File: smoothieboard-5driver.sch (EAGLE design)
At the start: 283 parts, among them IC1 LPC1769, IC10 LM1117-3.3V, IC11 78L12F, IC12 A4982, IC13 R-78E-5.0, IC2 A4982, IC3 A4982, IC4 MCP44X1, IC5 A4982, IC6 A4982, IC9 MCP44X1, J10 POWER_JACKSMD, Q1 BSL207SP, Q10 SUD50P04-08-GE3, Q2 12MHz, Q3 25MHz, Q4 ZXMN4A06, Q5 AOT240L, Q6 AOT240L, Q7 AOT240L, Q8 ZXMN4A06, Q9 ZXMN4A06, U1 USD-SOCKETNEW, X14 USBPTH

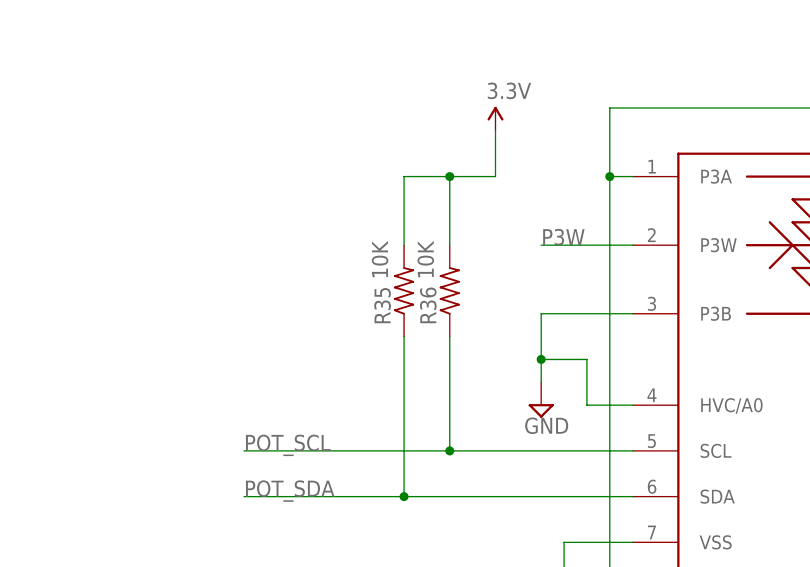
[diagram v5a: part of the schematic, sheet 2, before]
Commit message: reduce I2C pull-up resistors to 2.2k
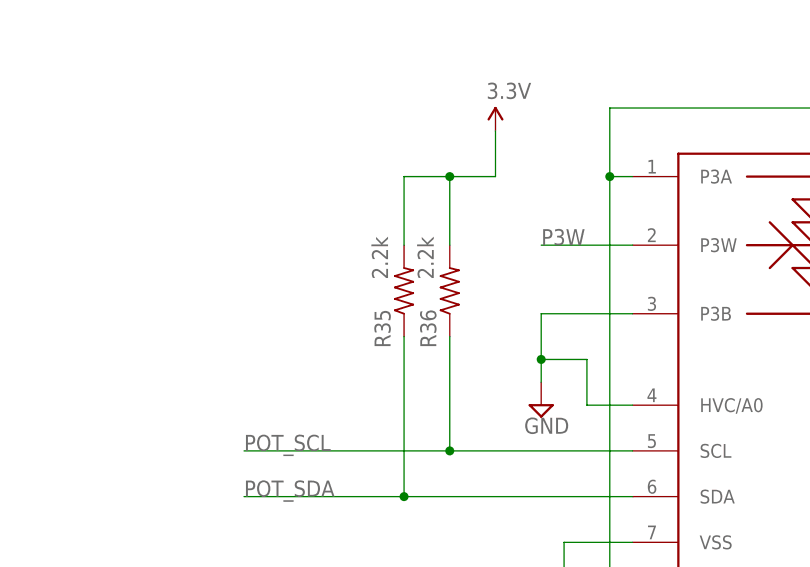
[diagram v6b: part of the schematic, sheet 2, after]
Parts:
- R35, R36, R5, R6: value 10K -> 2.2k
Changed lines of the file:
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@@
 <grid distance="0.1" unitdist="inch" unit="inch" style="lines" multiple="1" display="no" altdistance="0.01" altunitdist="inch" altunit="inch"/>
 <layers>
-<layer number="1" name="Top" color="4" fill="1" visible="yes" active="no"/>
-<layer number="2" name="Route2" color="2" fill="1" visible="yes" active="no"/>
-<layer number="3" name="Route3" color="4" fill="3" visible="yes" active="no"/>
-<layer number="4" name="Route4" color="1" fill="4" visible="yes" active="no"/>
-<layer number="5" name="Route5" color="4" fill="4" visible="yes" active="no"/>
-<layer number="6" name="Route6" color="1" fill="8" visible="yes" active="no"/>
-<layer number="7" name="Route7" color="4" fill="8" visible="yes" active="no"/>
-<layer number="8" name="Route8" color="1" fill="2" visible="yes" active="no"/>
-<layer number="9" name="Route9" color="4" fill="2" visible="yes" active="no"/>
-<layer number="10" name="Route10" color="1" fill="7" visible="yes" active="no"/>
-<layer number="11" name="Route11" color="4" fill="7" visible="yes" active="no"/>
-<layer number="12" name="Route12" color="1" fill="5" visible="yes" active="no"/>
-<layer number="13" name="Route13" color="4" fill="5" visible="yes" active="no"/>
-<layer number="14" name="Route14" color="1" fill="6" visible="yes" active="no"/>
-<layer number="15" name="Route15" color="5" fill="1" visible="yes" active="no"/>
-<layer number="16" name="Bottom" color="1" fill="1" visible="yes" active="no"/>
-<layer number="17" name="Pads" color="2" fill="1" visible="yes" active="no"/>
-<layer number="18" name="Vias" color="6" fill="1" visible="yes" active="no"/>
-<layer number="19" name="Unrouted" color="6" fill="1" visible="yes" active="no"/>
-<layer number="20" name="Dimension" color="15" fill="1" visible="yes" active="no"/>
-<layer number="21" name="tPlace" color="7" fill="1" visible="yes" active="no"/>
-<layer number="22" name="bPlace" color="7" fill="1" visible="yes" active="no"/>
-<layer number="23" name="tOrigins" color="15" fill="1" visible="yes" active="no"/>
-<layer number="24" name="bOrigins" color="15" fill="1" visible="yes" active="no"/>
-<layer number="25" name="tNames" color="7" fill="1" visible="yes" active="no"/>
-<layer number="26" name="bNames" color="7" fill="1" visible="yes" active="no"/>
-<layer number="27" name="tValues" color="7" fill="1" visible="yes" active="no"/>
-<layer number="28" name="bValues" color="7" fill="1" visible="yes" active="no"/>
+<layer number="1" name="Top" color="4" fill="1" visible="no" active="no"/>
+<layer number="2" name="Route2" color="2" fill="1" visible="no" active="no"/>
+<layer number="3" name="Route3" color="4" fill="3" visible="no" active="no"/>
+<layer number="4" name="Route4" color="1" fill="4" visible="no" active="no"/>
+<layer number="5" name="Route5" color="4" fill="4" visible="no" active="no"/>
+<layer number="6" name="Route6" color="1" fill="8" visible="no" active="no"/>
+<layer number="7" name="Route7" color="4" fill="8" visible="no" active="no"/>
+<layer number="8" name="Route8" color="1" fill="2" visible="no" active="no"/>
+<layer number="9" name="Route9" color="4" fill="2" visible="no" active="no"/>
+<layer number="10" name="Route10" color="1" fill="7" visible="no" active="no"/>
+<layer number="11" name="Route11" color="4" fill="7" visible="no" active="no"/>
+<layer number="12" name="Route12" color="1" fill="5" visible="no" active="no"/>
+<layer number="13" name="Route13" color="4" fill="5" visible="no" active="no"/>
+<layer number="14" name="Route14" color="1" fill="6" visible="no" active="no"/>
+<layer number="15" name="Route15" color="5" fill="1" visible="no" active="no"/>
+<layer number="16" name="Bottom" color="1" fill="1" visible="no" active="no"/>
+<layer number="17" name="Pads" color="2" fill="1" visible="no" active="no"/>
+<layer number="18" name="Vias" color="6" fill="1" visible="no" active="no"/>
+<layer number="19" name="Unrouted" color="6" fill="1" visible="no" active="no"/>
+<layer number="20" name="Dimension" color="15" fill="1" visible="no" active="no"/>
+<layer number="21" name="tPlace" color="7" fill="1" visible="no" active="no"/>
+<layer number="22" name="bPlace" color="7" fill="1" visible="no" active="no"/>
+<layer number="23" name="tOrigins" color="15" fill="1" visible="no" active="no"/>
+<layer number="24" name="bOrigins" color="15" fill="1" visible="no" active="no"/>
+<layer number="25" name="tNames" color="7" fill="1" visible="no" active="no"/>
+<layer number="26" name="bNames" color="7" fill="1" visible="no" active="no"/>
+<layer number="27" name="tValues" color="7" fill="1" visible="no" active="no"/>
+<layer number="28" name="bValues" color="7" fill="1" visible="no" active="no"/>
 <layer number="29" name="tStop" color="7" fill="3" visible="no" active="no"/>
 <layer number="30" name="bStop" color="7" fill="6" visible="no" active="no"/>
@@
 <layer number="35" name="tGlue" color="7" fill="4" visible="no" active="no"/>
 <layer number="36" name="bGlue" color="7" fill="5" visible="no" active="no"/>
-<layer number="37" name="tTest" color="7" fill="1" visible="yes" active="no"/>
-<layer number="38" name="bTest" color="7" fill="1" visible="yes" active="no"/>
+<layer number="37" name="tTest" color="7" fill="1" visible="no" active="no"/>
+<layer number="38" name="bTest" color="7" fill="1" visible="no" active="no"/>
 <layer number="39" name="tKeepout" color="4" fill="11" visible="no" active="no"/>
 <layer number="40" name="bKeepout" color="1" fill="11" visible="no" active="no"/>
@@
 <layer number="44" name="Drills" color="7" fill="1" visible="no" active="no"/>
 <layer number="45" name="Holes" color="7" fill="1" visible="no" active="no"/>
-<layer number="46" name="Milling" color="3" fill="1" visible="yes" active="no"/>
-<layer number="47" name="Measures" color="7" fill="1" visible="yes" active="no"/>
-<layer number="48" name="Document" color="7" fill="1" visible="yes" active="no"/>
-<layer number="49" name="Reference" color="7" fill="1" visible="yes" active="no"/>
-<layer number="50" name="dxf" color="7" fill="1" visible="yes" active="no"/>
-<layer number="51" name="tDocu" color="7" fill="1" visible="yes" active="no"/>
-<layer number="52" name="bDocu" color="7" fill="1" visible="yes" active="no"/>
-<layer number="53" name="tGND_GNDA" color="7" fill="9" visible="yes" active="no"/>
-<layer number="54" name="bGND_GNDA" color="1" fill="9" visible="yes" active="no"/>
-<layer number="56" name="wert" color="7" fill="1" visible="yes" active="no"/>
+<layer number="46" name="Milling" color="3" fill="1" visible="no" active="no"/>
+<layer number="47" name="Measures" color="7" fill="1" visible="no" active="no"/>
+<layer number="48" name="Document" color="7" fill="1" visible="no" active="no"/>
+<layer number="49" name="Reference" color="7" fill="1" visible="no" active="no"/>
+<layer number="50" name="dxf" color="7" fill="1" visible="no" active="no"/>
+<layer number="51" name="tDocu" color="7" fill="1" visible="no" active="no"/>
+<layer number="52" name="bDocu" color="7" fill="1" visible="no" active="no"/>
+<layer number="53" name="tGND_GNDA" color="7" fill="9" visible="no" active="no"/>
+<layer number="54" name="bGND_GNDA" color="1" fill="9" visible="no" active="no"/>
+<layer number="56" name="wert" color="7" fill="1" visible="no" active="no"/>
 <layer number="91" name="Nets" color="2" fill="1" visible="yes" active="yes"/>
 <layer number="92" name="Busses" color="1" fill="1" visible="yes" active="yes"/>
@@
 <part name="SUPPLY61" library="supply2" deviceset="GND" device=""/>
 <part name="P+30" library="SparkFun" deviceset="3.3V" device=""/>
-<part name="R5" library="resistor" deviceset="R-US_" device="R0603" value="10K"/>
-<part name="R6" library="resistor" deviceset="R-US_" device="R0603" value="10K"/>
+<part name="R5" library="resistor" deviceset="R-US_" device="R0603" value="2.2k"/>
+<part name="R6" library="resistor" deviceset="R-US_" device="R0603" value="2.2k"/>
 <part name="SUPPLY64" library="supply2" deviceset="GND" device=""/>
 <part name="S1" library="SparkFun" deviceset="TAC_SWITCH" device="SMD"/>
@@
 <part name="RN1" library="resistor-dil" deviceset="4R-N" device="0603-ARV" value="4.7K"/>
 <part name="IC4" library="Geos" deviceset="MCP44X1" device=""/>
-<part name="R35" library="resistor" deviceset="R-US_" device="R0603" value="10K"/>
-<part name="R36" library="resistor" deviceset="R-US_" device="R0603" value="10K"/>
+<part name="R35" library="resistor" deviceset="R-US_" device="R0603" value="2.2k"/>
+<part name="R36" library="resistor" deviceset="R-US_" device="R0603" value="2.2k"/>
 <part name="J1" library="con-amp" deviceset="MTA04-100" device=""/>
 <part name="J2" library="con-amp" deviceset="MTA04-100" device=""/>
@@
 <instance part="IC4" gate="G$1" x="289.56" y="71.12"/>
 <instance part="R35" gate="G$1" x="259.08" y="127" smashed="yes" rot="R90">
-<attribute name="NAME" x="257.5814" y="123.19" size="1.778" layer="95" rot="R90"/>
+<attribute name="NAME" x="257.5814" y="120.65" size="1.778" layer="95" rot="R90"/>
 <attribute name="VALUE" x="257.302" y="128.27" size="1.778" layer="96" rot="R90"/>
 </instance>
 <instance part="R36" gate="G$1" x="264.16" y="127" smashed="yes" rot="R90">
-<attribute name="NAME" x="262.6614" y="123.19" size="1.778" layer="95" rot="R90"/>
+<attribute name="NAME" x="262.6614" y="120.65" size="1.778" layer="95" rot="R90"/>
 <attribute name="VALUE" x="262.382" y="128.27" size="1.778" layer="96" rot="R90"/>
 </instance>

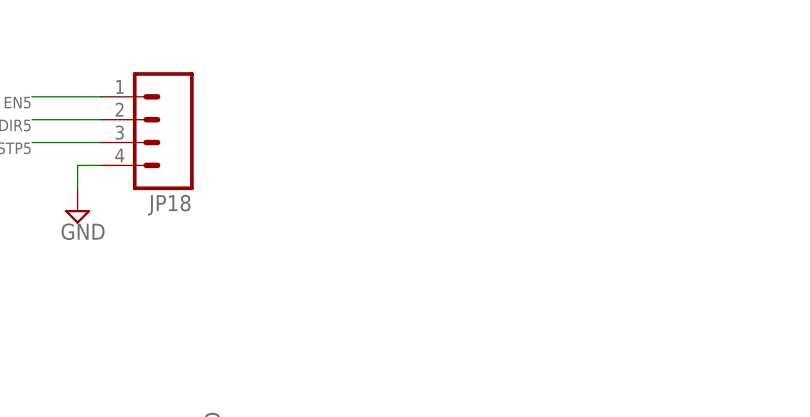
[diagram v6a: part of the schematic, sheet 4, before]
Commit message: Break out digipot I2C bus to a header
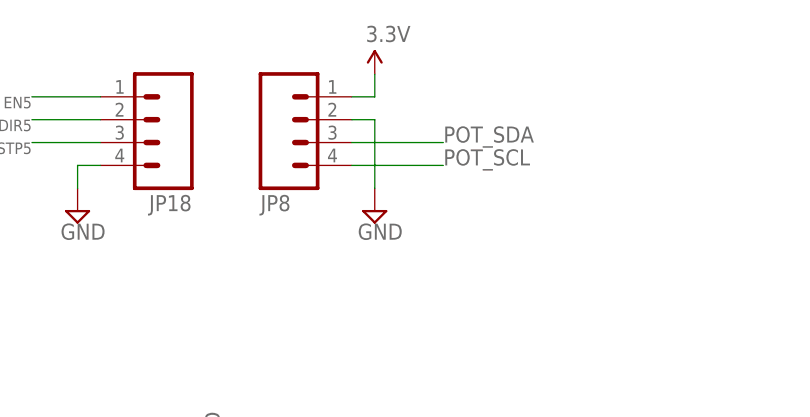
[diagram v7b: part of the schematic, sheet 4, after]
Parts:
- added JP8: (no value), SparkFun:M041X04_NO_SILK
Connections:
- net 3.3V: now also JP8.1
- net GND: now also JP8.2
- net POT_SCL: now also JP8.4
- net POT_SDA: now also JP8.3
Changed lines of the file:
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@@
 <attribute name="OC_NEWARK" value="unknown"/>
 </part>
+<part name="JP8" library="SparkFun" deviceset="M04" device="1X04_NO_SILK"/>
+<part name="P+38" library="SparkFun" deviceset="3.3V" device=""/>
+<part name="SUPPLY86" library="supply2" deviceset="GND" device=""/>
 </parts>
 <sheets>
@@
 <instance part="X16" gate="G$1" x="294.64" y="203.2"/>
 <instance part="X17" gate="G$1" x="182.88" y="185.42" rot="R180"/>
+<instance part="JP8" gate="G$1" x="124.46" y="243.84" rot="MR180"/>
+<instance part="P+38" gate="G$1" x="132.08" y="248.92"/>
+<instance part="SUPPLY86" gate="GND" x="132.08" y="233.68"/>
 </instances>
 <busses>
@@
 <pinref part="R81" gate="G$1" pin="2"/>
 </segment>
+<segment>
+<pinref part="JP8" gate="G$1" pin="1"/>
+<pinref part="P+38" gate="G$1" pin="3.3V"/>
+<wire x1="129.54" y1="246.38" x2="132.08" y2="246.38" width="0.1524" layer="91"/>
+<wire x1="132.08" y1="246.38" x2="132.08" y2="248.92" width="0.1524" layer="91"/>
+</segment>
 </net>
 <net name="GND" class="0">
@@
 <wire x1="236.22" y1="91.44" x2="236.22" y2="93.98" width="0.1524" layer="91"/>
 </segment>
+<segment>
+<pinref part="JP8" gate="G$1" pin="2"/>
+<pinref part="SUPPLY86" gate="GND" pin="GND"/>
+<wire x1="129.54" y1="243.84" x2="132.08" y2="243.84" width="0.1524" layer="91"/>
+<wire x1="132.08" y1="243.84" x2="132.08" y2="236.22" width="0.1524" layer="91"/>
+</segment>
 </net>
 <net name="N$29" class="0">
@@
 <pinref part="IC9" gate="G$1" pin="SCL"/>
 </segment>
+<segment>
+<pinref part="JP8" gate="G$1" pin="4"/>
+<wire x1="129.54" y1="238.76" x2="139.7" y2="238.76" width="0.1524" layer="91"/>
+<label x="139.7" y="238.76" size="1.778" layer="95"/>
+</segment>
 </net>
 <net name="POT_SDA" class="0">
@@
 <pinref part="IC9" gate="G$1" pin="SDA"/>
 </segment>
+<segment>
+<pinref part="JP8" gate="G$1" pin="3"/>
+<wire x1="129.54" y1="241.3" x2="139.7" y2="241.3" width="0.1524" layer="91"/>
+<label x="139.7" y="241.3" size="1.778" layer="95"/>
+</segment>
 </net>

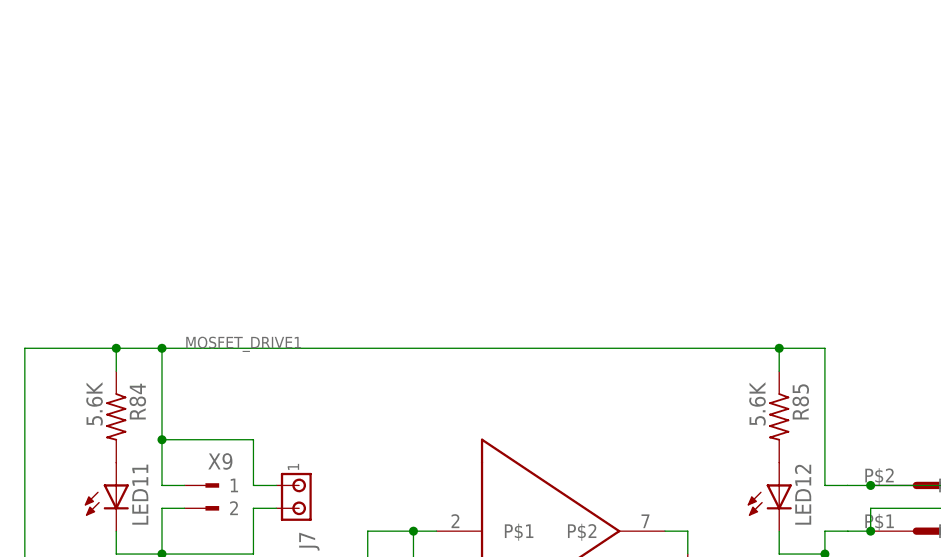
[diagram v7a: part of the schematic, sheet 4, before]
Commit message: add jumper for VBB power to new mosfets
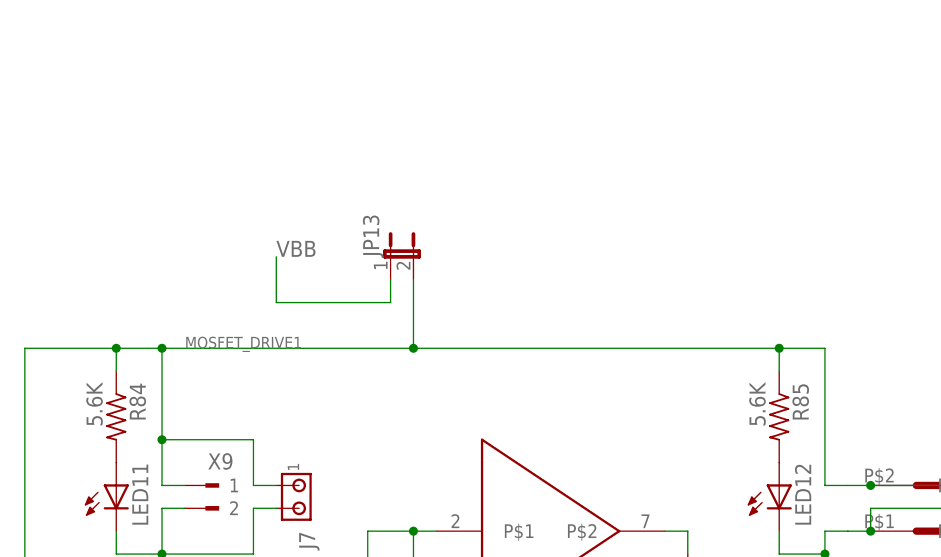
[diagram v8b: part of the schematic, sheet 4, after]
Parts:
- added JP13: (no value), jumper:JP1E
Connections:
- net MOSFET_DRIVE1: now also JP13.2
- net VBB: now also JP13.1
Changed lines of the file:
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@@
 <part name="P+38" library="SparkFun" deviceset="3.3V" device=""/>
 <part name="SUPPLY86" library="supply2" deviceset="GND" device=""/>
+<part name="JP13" library="jumper" deviceset="JP1E" device=""/>
 </parts>
 <sheets>
@@
 <instance part="P+38" gate="G$1" x="132.08" y="248.92"/>
 <instance part="SUPPLY86" gate="GND" x="132.08" y="233.68"/>
+<instance part="JP13" gate="A" x="226.06" y="228.6"/>
 </instances>
 <busses>
@@
 <wire x1="200.66" y1="104.14" x2="200.66" y2="111.76" width="0.1524" layer="91"/>
 </segment>
+<segment>
+<wire x1="213.36" y1="228.6" x2="213.36" y2="223.52" width="0.1524" layer="91"/>
+<pinref part="JP13" gate="A" pin="1"/>
+<wire x1="213.36" y1="223.52" x2="226.06" y2="223.52" width="0.1524" layer="91"/>
+<wire x1="226.06" y1="223.52" x2="226.06" y2="226.06" width="0.1524" layer="91"/>
+<label x="213.36" y="228.6" size="1.778" layer="95"/>
+</segment>
 </net>
 <net name="MS2" class="0">
@@
 <wire x1="276.86" y1="203.2" x2="274.32" y2="203.2" width="0.4064" layer="91"/>
 <wire x1="274.32" y1="218.44" x2="274.32" y2="203.2" width="0.4064" layer="91"/>
-<wire x1="200.66" y1="218.44" x2="269.24" y2="218.44" width="0.4064" layer="91"/>
+<wire x1="200.66" y1="218.44" x2="228.6" y2="218.44" width="0.4064" layer="91"/>
+<wire x1="228.6" y1="218.44" x2="269.24" y2="218.44" width="0.4064" layer="91"/>
 <wire x1="269.24" y1="218.44" x2="274.32" y2="218.44" width="0.4064" layer="91"/>
 <pinref part="R85" gate="G$1" pin="1"/>
@@
 <pinref part="X17" gate="G$1" pin="2"/>
 <junction x="185.42" y="187.96"/>
+<pinref part="JP13" gate="A" pin="2"/>
+<wire x1="228.6" y1="226.06" x2="228.6" y2="218.44" width="0.1524" layer="91"/>
+<junction x="228.6" y="218.44"/>
 </segment>
 </net>
